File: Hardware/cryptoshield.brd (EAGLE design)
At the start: 59.7 x 53.3 mm, 45 parts, among them J1 AVR_SPI_PRG_6PTH, Q1 BSS138, Q2 BSS138, U1 33mhz

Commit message: changed name of part
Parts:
- C10: value 1000uF -> 0.1uF; device SparkFun-Passives:0603-CAP -> SparkFun-Capacitors:0603-CAP
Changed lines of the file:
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@@
 <attribute name="VALUE" value="10uF" x="17.78" y="6.604" size="1.778" layer="27" display="off"/>
 </element>
-<element name="C10" library="SparkFun-Passives" package="0603-CAP" value="1000uF" x="13.97" y="6.858" rot="R270"/>
+<element name="C10" library="SparkFun-Capacitors" package="0603-CAP" value="0.1uF" x="13.97" y="6.858" rot="R270">
+<attribute name="PROD_ID" value="CAP-00810" x="13.97" y="6.858" size="1.778" layer="27" rot="R270" display="off"/>
+<attribute name="VALUE" value="0.1uF" x="13.97" y="6.858" size="1.778" layer="27" rot="R270" display="off"/>
+</element>
 <element name="JP2" library="SparkFun-Connectors" package="1X03" value="" x="34.29" y="39.37" smashed="yes" rot="R270">
 <attribute name="VALUE" x="31.115" y="40.64" size="1.27" layer="27" rot="R270"/>

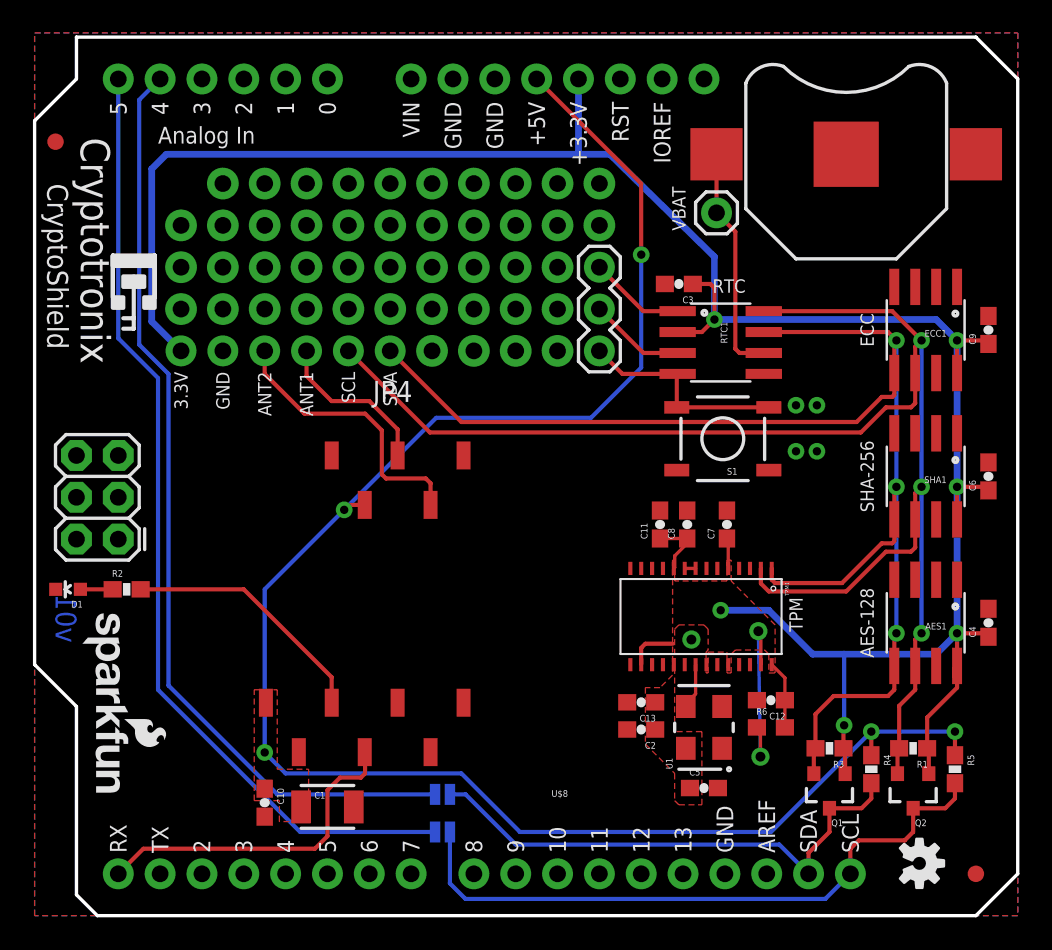
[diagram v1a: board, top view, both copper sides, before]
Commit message: Changes 5V to IOREF
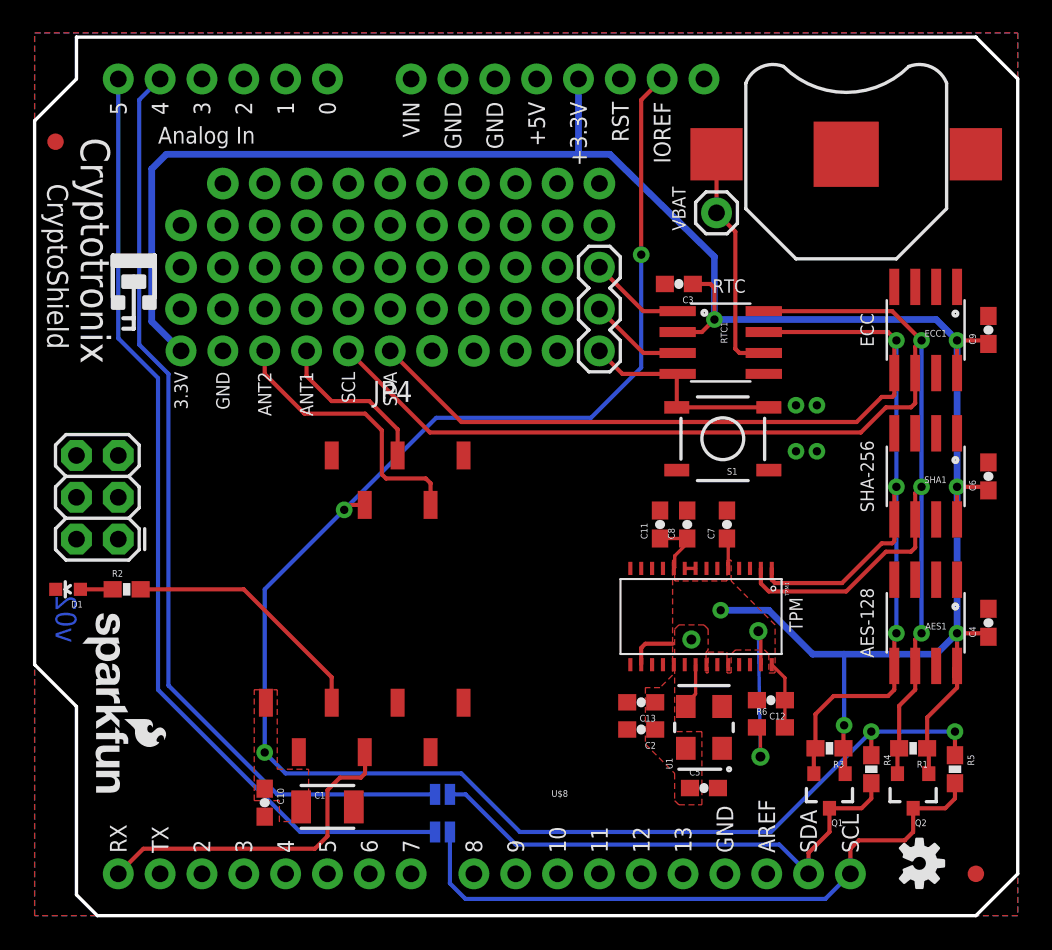
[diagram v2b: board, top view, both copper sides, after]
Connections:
- removed net 5V: C1.1, C10.1, R4.1, R5.1, U$1.5V, U$8.11, U$8.2
- new net VCCIO: C1.1, C10.1, R4.1, R5.1, U$1.IOREF, U$8.11, U$8.2
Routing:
- net 5V: track 109.2 -> 0.00 mm, vias 5 -> 0
- net VCCIO: track 0.00 -> 107.1 mm, vias 0 -> 5
- added copper zone on layer 1, net VCCIO
- removed copper zone on layer 1, net 5V
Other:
- board text added: "v02"
- board text removed: "v01"

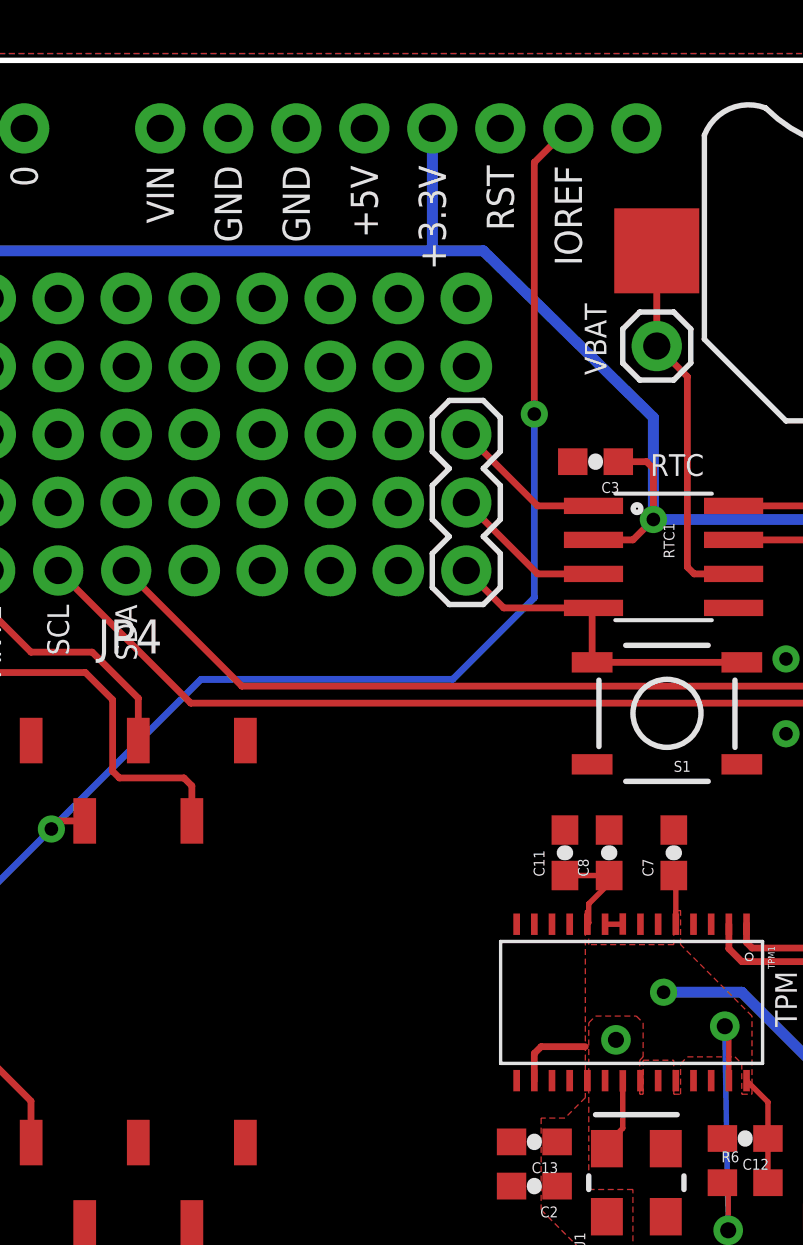
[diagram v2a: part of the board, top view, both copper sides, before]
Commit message: added mosfet reset circuit to couple TPM reset to Arduino Reset pin
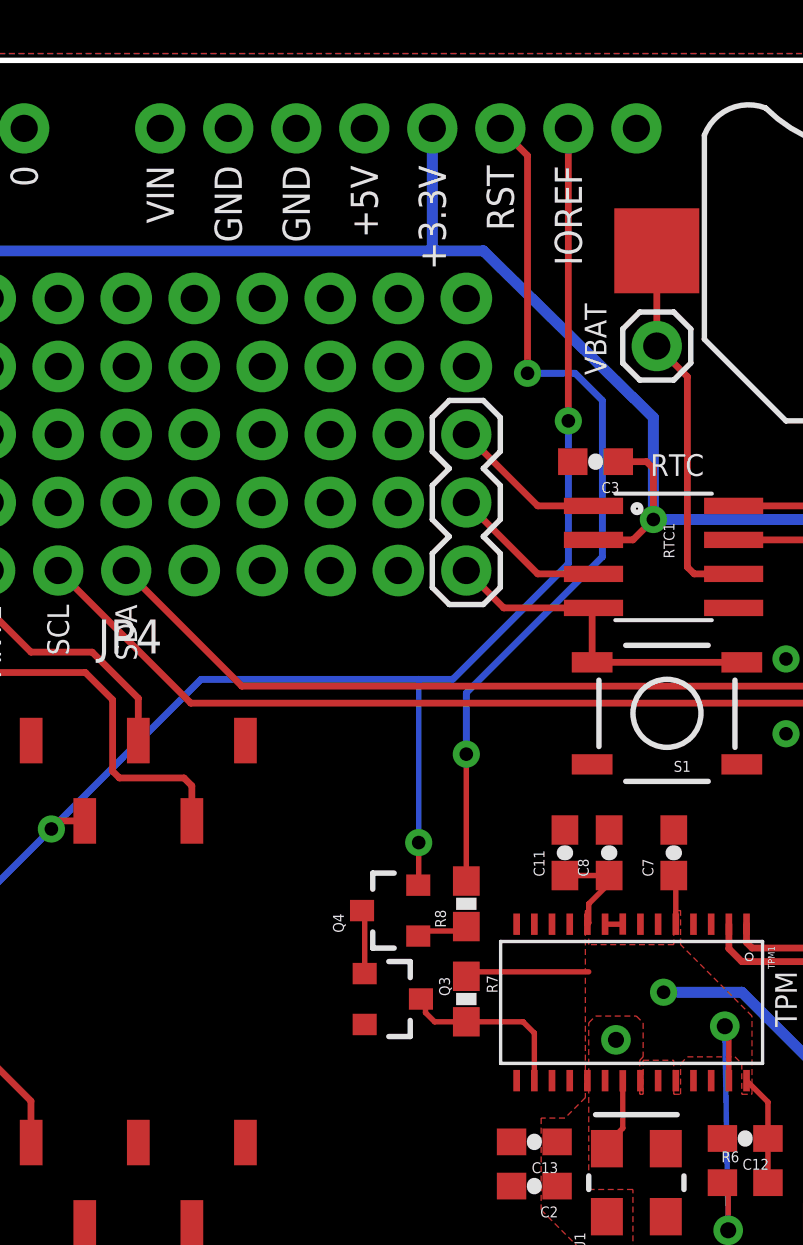
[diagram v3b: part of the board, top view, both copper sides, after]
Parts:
- added Q3: BSS138, SparkFun-DiscreteSemi:SOT23-3
- added Q4: MOSFET-PCH, SparkFun-DiscreteSemi:SOT23-3
- added R7, R8: 10K, SparkFun:0603-RES
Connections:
- new net !RESET: R8.2, U$1.RES
- new net N$18: Q3.3, R7.2, TPM1.16
- new net N$20: Q3.1, Q4.3
- new net N$21: Q4.1, R8.1
- net 3.3V: now also R7.1; no longer TPM1.16
- net GND: now also Q3.2
- net VCCIO: now also Q4.2
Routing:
- net !RESET: track 0.00 -> 32.8 mm, vias 0 -> 2
- net VCCIO: track 107.1 -> 114.8 mm, vias 5 -> 6
- net N$18: track 0.00 -> 6.74 mm
- net N$20: track 0.00 -> 2.39 mm
- net N$21: track 0.00 -> 2.13 mm
- net 3.3V: track 151.9 -> 153.6 mm
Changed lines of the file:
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@@
 <?xml version="1.0" encoding="utf-8"?>
 <!DOCTYPE eagle SYSTEM "eagle.dtd">
-<eagle version="6.4">
+<eagle version="6.5.0">
 <drawing>
 <settings>
@@
 <element name="SJ1" library="SparkFun-Passives" package="PAD-JUMPER-2-NO_YES_SILK" value="" x="24.765" y="7.366" rot="MR0"/>
 <element name="SJ2" library="SparkFun-Passives" package="PAD-JUMPER-2-NO_YES_SILK" value="" x="24.765" y="5.08" rot="MR0"/>
+<element name="Q3" library="SparkFun-DiscreteSemi" package="SOT23-3" value="BSS138" x="31.496" y="18.288" rot="R270">
+<attribute name="PROD_ID" value="TRANS-00830" x="31.496" y="18.288" size="1.778" layer="27" rot="R270" display="off"/>
+</element>
+<element name="R7" library="SparkFun" package="0603-RES" value="10K" x="34.29" y="18.288" rot="R270"/>
+<element name="Q4" library="SparkFun-DiscreteSemi" package="SOT23-3" value="MOSFET-PCH" x="31.496" y="21.59" rot="R90">
+<attribute name="PROD_ID" value="TRANS-08285" x="31.496" y="21.59" size="1.778" layer="27" rot="R90" display="off"/>
+</element>
+<element name="R8" library="SparkFun" package="0603-RES" value="10K" x="34.29" y="21.844" rot="R90"/>
 </elements>
 <signals>
@@
 <via x="47.498" y="30.988" extent="1-16" drill="0.508"/>
 <via x="47.498" y="28.194" extent="1-16" drill="0.508"/>
+<contactref element="Q3" pad="2"/>
 </signal>
 <signal name="RST">
@@
 <contactref element="R1" pad="1"/>
 <contactref element="Q2" pad="1"/>
-<contactref element="TPM1" pad="16"/>
 <wire x1="45.554" y1="11.43" x2="45.554" y2="13.081" width="0.2032" layer="1"/>
 <wire x1="45.554" y1="13.081" x2="45.554" y2="14.4408" width="0.2032" layer="1"/>
@@
 <wire x1="55.88" y1="15.0368" x2="56.007" y2="15.1638" width="0.254" layer="1"/>
 <wire x1="33.02" y1="46.355" x2="33.147" y2="46.228" width="0.4064" layer="16"/>
-<wire x1="36.83" y1="15.24" x2="36.83" y2="16.256" width="0.254" layer="1"/>
-<wire x1="36.83" y1="16.256" x2="37.084" y2="16.51" width="0.254" layer="1"/>
-<wire x1="37.084" y1="16.51" x2="38.735" y2="16.51" width="0.254" layer="1"/>
 <wire x1="41.275" y1="36.195" x2="54.737" y2="36.195" width="0.4064" layer="16"/>
 <wire x1="54.737" y1="36.195" x2="56.007" y2="34.925" width="0.4064" layer="16"/>
+<contactref element="R7" pad="1"/>
+<wire x1="34.29" y1="19.138" x2="34.456" y2="19.304" width="0.2032" layer="1"/>
+<wire x1="34.456" y1="19.304" x2="38.862" y2="19.304" width="0.2032" layer="1"/>
 </signal>
 <signal name="32KHZ">
@@
 <wire x1="18.796" y1="24.638" x2="13.97" y2="19.812" width="0.254" layer="16"/>
 <wire x1="13.97" y1="19.812" x2="13.97" y2="9.906" width="0.254" layer="16"/>
-<via x="36.83" y="40.132" extent="1-16" drill="0.508"/>
-<wire x1="36.83" y1="40.132" x2="36.83" y2="33.274" width="0.254" layer="16"/>
-<wire x1="36.83" y1="33.274" x2="33.782" y2="30.226" width="0.254" layer="16"/>
-<wire x1="33.782" y1="30.226" x2="24.384" y2="30.226" width="0.254" layer="16"/>
+<via x="38.1" y="39.878" extent="1-16" drill="0.508"/>
+<wire x1="38.1" y1="39.878" x2="38.1" y2="34.544" width="0.254" layer="16"/>
+<wire x1="38.1" y1="34.544" x2="33.782" y2="30.226" width="0.254" layer="16"/>
+<wire x1="33.782" y1="30.226" x2="32.512" y2="30.226" width="0.254" layer="16"/>
+<wire x1="32.512" y1="30.226" x2="24.384" y2="30.226" width="0.254" layer="16"/>
 <wire x1="24.384" y1="30.226" x2="18.796" y2="24.638" width="0.254" layer="16"/>
-<wire x1="36.83" y1="40.132" x2="36.83" y2="49.53" width="0.254" layer="1"/>
-<wire x1="36.83" y1="49.53" x2="38.1" y2="50.8" width="0.254" layer="1"/>
+<wire x1="38.1" y1="39.878" x2="38.1" y2="50.8" width="0.254" layer="1"/>
+<contactref element="Q4" pad="2"/>
+<wire x1="32.496" y1="22.54" x2="32.512" y2="22.556" width="0.2032" layer="1"/>
+<wire x1="32.512" y1="22.556" x2="32.512" y2="24.13" width="0.2032" layer="1"/>
+<via x="32.512" y="24.13" extent="1-16" drill="0.508"/>
+<wire x1="32.512" y1="24.13" x2="32.512" y2="30.226" width="0.2032" layer="16"/>
+</signal>
+<signal name="N$18">
+<contactref element="TPM1" pad="16"/>
+<contactref element="R7" pad="2"/>
+<contactref element="Q3" pad="3"/>
+<wire x1="36.83" y1="15.24" x2="36.83" y2="17.018" width="0.2032" layer="1"/>
+<wire x1="36.83" y1="17.018" x2="36.41" y2="17.438" width="0.2032" layer="1"/>
+<wire x1="36.41" y1="17.438" x2="34.29" y2="17.438" width="0.2032" layer="1"/>
+<wire x1="32.596" y1="18.288" x2="32.766" y2="18.118" width="0.2032" layer="1"/>
+<wire x1="32.766" y1="18.118" x2="32.766" y2="17.78" width="0.2032" layer="1"/>
+<wire x1="32.766" y1="17.78" x2="33.108" y2="17.438" width="0.2032" layer="1"/>
+<wire x1="33.108" y1="17.438" x2="34.29" y2="17.438" width="0.2032" layer="1"/>
+</signal>
+<signal name="N$20">
+<contactref element="Q3" pad="1"/>
+<contactref element="Q4" pad="3"/>
+<wire x1="30.396" y1="21.59" x2="30.496" y2="21.49" width="0.2032" layer="1"/>
+<wire x1="30.496" y1="21.49" x2="30.496" y2="19.238" width="0.2032" layer="1"/>
+</signal>
+<signal name="N$21">
+<contactref element="Q4" pad="1"/>
+<contactref element="R8" pad="1"/>
+<wire x1="32.496" y1="20.64" x2="32.684" y2="20.828" width="0.2032" layer="1"/>
+<wire x1="32.684" y1="20.828" x2="34.29" y2="20.828" width="0.2032" layer="1"/>
+<wire x1="34.29" y1="20.828" x2="34.29" y2="20.994" width="0.2032" layer="1"/>
+<wire x1="34.29" y1="21.082" x2="34.29" y2="20.994" width="0.2032" layer="1"/>
+</signal>
+<signal name="!RESET">
+<contactref element="R8" pad="2"/>
+<contactref element="U$1" pad="RES"/>
+<wire x1="35.56" y1="50.8" x2="36.576" y2="49.784" width="0.254" layer="1"/>
+<wire x1="36.576" y1="49.784" x2="36.576" y2="41.656" width="0.254" layer="1"/>
+<via x="36.576" y="41.656" extent="1-16" drill="0.508"/>
+<wire x1="36.576" y1="41.656" x2="38.354" y2="41.656" width="0.254" layer="16"/>
+<wire x1="38.354" y1="41.656" x2="39.37" y2="40.64" width="0.254" layer="16"/>
+<wire x1="39.37" y1="40.64" x2="39.37" y2="34.798" width="0.254" layer="16"/>
+<wire x1="39.37" y1="34.798" x2="34.29" y2="29.718" width="0.254" layer="16"/>
+<wire x1="34.29" y1="29.718" x2="34.29" y2="27.432" width="0.254" layer="16"/>
+<via x="34.29" y="27.432" extent="1-16" drill="0.508"/>
+<wire x1="34.29" y1="22.694" x2="34.29" y2="27.432" width="0.2032" layer="1"/>
 </signal>
 </signals>
